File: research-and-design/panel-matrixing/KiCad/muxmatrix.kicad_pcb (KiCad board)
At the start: 2 copper layers, 112 parts, among them P1 CONN_01X03, P10 CONN_01X03, P11 CONN_01X03, P12 CONN_01X03, P13 CONN_01X03, P14 CONN_01X03, P15 CONN_01X03, P16 CONN_01X03, P17 CONN_01X03, P18 CONN_01X03, P19 CONN_01X03, P2 CONN_01X03, P20 CONN_01X03, P21 CONN_01X07, P22 CONN_01X03, P23 CONN_01X03, P24 CONN_01X03, P25 CONN_01X03, P26 CONN_01X03, P27 CONN_01X03, P28 CONN_01X03, P29 CONN_01X03, P3 CONN_01X03, P30 CONN_01X03, P31 CONN_01X03, P32 CONN_01X03, P33 CONN_01X03, P4 CONN_01X03, P5 CONN_01X03, P6 CONN_01X03, P7 CONN_01X03, P8 CONN_01X03, P9 CONN_01X03, U1 4052, U10 4052, U2 4052, U3 4052, U4 4052, U5 4052, U6 4052, U7 4052, U8 4052, U9 4052

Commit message: worked on layout
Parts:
- removed U10, U6, U7, U8, U9: 4052, SMD_Packages:SO-16-L
- P21: value CONN_01X07 -> CONN_01X03
- P33: value CONN_01X03 -> CONN_01X07
- U1, U2, U3, U4, U5: footprint SMD_Packages:SO-16-L -> SMD_Packages:SO-16-N
- moved U1 146.1 mm to (207.0, 31.8)
- moved U2 134.6 mm to (218.4, 33.0)
- moved U3 121.9 mm to (229.9, 33.0)
- moved U4 109.2 mm to (241.3, 31.8)
- moved U5 100.3 mm to (252.7, 31.8)
- moved C1 44.5 mm to (243.8, 62.2)
- moved C3 44.5 mm to (243.8, 59.7)
- moved C4 44.5 mm to (243.8, 53.3)
- moved C5 44.5 mm to (243.8, 50.8)
- moved C2 44.4 mm to (243.8, 55.9)
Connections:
- P10 pad 2: K21 -> K10
- P11 pad 2: K6 -> K11
- P12 pad 2: K22 -> K12
- P13 pad 2: K7 -> K13
- P14 pad 2: K23 -> K14
- P15 pad 2: K8 -> K15
- P16 pad 2: K24 -> K16
- P17 pad 2: K9 -> K17
- P18 pad 2: K25 -> K18
- P19 pad 2: K10 -> K19
- P2 pad 2: K17 -> K2
- P20 pad 2: K26 -> K20
- P21 pad 1: VDD -> Net-(P21-Pad1)
- P21 pad 2: GND -> K21
- P21 pad 3: A0 -> Net-(P21-Pad3)
- P21 pad 4: A1 -> (no net)
- P21 pad 5: EN -> (no net)
- P21 pad 6: A -> (no net)
- P21 pad 7: B -> (no net)
- P22 pad 2: K11 -> K22
- P23 pad 2: K27 -> K23
- P24 pad 2: K12 -> K24
- P25 pad 2: K28 -> K25
- P26 pad 2: K13 -> K26
- P27 pad 2: K29 -> K27
- P28 pad 2: K14 -> K28
- P29 pad 2: K30 -> K29
- P3 pad 2: K2 -> K3
- P30 pad 2: K15 -> K30
- P32 pad 2: K16 -> K32
- P33 pad 1: Net-(P33-Pad1) -> VDD
- P33 pad 2: K32 -> GND
- P33 pad 3: Net-(P33-Pad3) -> A0
- P4 pad 2: K18 -> K4
- P5 pad 2: K3 -> K5
- P6 pad 2: K19 -> K6
- P7 pad 2: K4 -> K7
- P8 pad 2: K20 -> K8
- P9 pad 2: K5 -> K9
- R10 pad 1: Net-(P5-Pad1) -> VDD
- R10 pad 2: GND -> Net-(P10-Pad3)
- R11 pad 2: Net-(P6-Pad3) -> Net-(P11-Pad3)
- R12 pad 1: Net-(P6-Pad1) -> VDD
- R12 pad 2: GND -> Net-(P12-Pad3)
- R13 pad 2: Net-(P7-Pad3) -> Net-(P13-Pad3)
- R14 pad 1: Net-(P7-Pad1) -> VDD
- R14 pad 2: GND -> Net-(P14-Pad3)
- R15 pad 2: Net-(P8-Pad3) -> Net-(P15-Pad3)
- R16 pad 1: Net-(P8-Pad1) -> VDD
- R16 pad 2: GND -> Net-(P16-Pad3)
- R17 pad 1: VDD -> Net-(P1-Pad1)
- R17 pad 2: Net-(P9-Pad3) -> GND
- R18 pad 1: Net-(P9-Pad1) -> Net-(P2-Pad1)
- R19 pad 1: VDD -> Net-(P3-Pad1)
- R19 pad 2: Net-(P10-Pad3) -> GND
- R2 pad 1: Net-(P1-Pad1) -> VDD
- R2 pad 2: GND -> Net-(P2-Pad3)
- R20 pad 1: Net-(P10-Pad1) -> Net-(P4-Pad1)
- R21 pad 1: VDD -> Net-(P5-Pad1)
- R21 pad 2: Net-(P11-Pad3) -> GND
- R22 pad 1: Net-(P11-Pad1) -> Net-(P6-Pad1)
- R23 pad 1: VDD -> Net-(P7-Pad1)
- R23 pad 2: Net-(P12-Pad3) -> GND
- R24 pad 1: Net-(P12-Pad1) -> Net-(P8-Pad1)
- R25 pad 1: VDD -> Net-(P9-Pad1)
- R25 pad 2: Net-(P13-Pad3) -> GND
- R26 pad 1: Net-(P13-Pad1) -> Net-(P10-Pad1)
- R27 pad 1: VDD -> Net-(P11-Pad1)
- R27 pad 2: Net-(P14-Pad3) -> GND
- R28 pad 1: Net-(P14-Pad1) -> Net-(P12-Pad1)
- R29 pad 1: VDD -> Net-(P13-Pad1)
- R29 pad 2: Net-(P15-Pad3) -> GND
- R3 pad 2: Net-(P2-Pad3) -> Net-(P3-Pad3)
- R30 pad 1: Net-(P15-Pad1) -> Net-(P14-Pad1)
- R31 pad 1: VDD -> Net-(P15-Pad1)
- R31 pad 2: Net-(P16-Pad3) -> GND
- R34 pad 1: Net-(P17-Pad1) -> VDD
- R34 pad 2: GND -> Net-(P18-Pad3)
- R35 pad 2: Net-(P18-Pad3) -> Net-(P19-Pad3)
- R36 pad 1: Net-(P18-Pad1) -> VDD
- R36 pad 2: GND -> Net-(P20-Pad3)
- R37 pad 2: Net-(P19-Pad3) -> Net-(P21-Pad3)
- R38 pad 1: Net-(P19-Pad1) -> VDD
- R38 pad 2: GND -> Net-(P22-Pad3)
- R39 pad 2: Net-(P20-Pad3) -> Net-(P23-Pad3)
- R4 pad 1: Net-(P2-Pad1) -> VDD
- R4 pad 2: GND -> Net-(P4-Pad3)
- R40 pad 1: Net-(P20-Pad1) -> VDD
- R40 pad 2: GND -> Net-(P24-Pad3)
- R41 pad 2: Net-(P22-Pad3) -> Net-(P25-Pad3)
- R42 pad 1: Net-(P22-Pad1) -> VDD
- R42 pad 2: GND -> Net-(P26-Pad3)
- R43 pad 2: Net-(P23-Pad3) -> Net-(P27-Pad3)
- R44 pad 1: Net-(P23-Pad1) -> VDD
- R44 pad 2: GND -> Net-(P28-Pad3)
- R45 pad 2: Net-(P24-Pad3) -> Net-(P29-Pad3)
- R46 pad 1: Net-(P24-Pad1) -> VDD
- R46 pad 2: GND -> Net-(P30-Pad3)
- R47 pad 2: Net-(P25-Pad3) -> Net-(P31-Pad3)
- R48 pad 1: Net-(P25-Pad1) -> VDD
- R48 pad 2: GND -> Net-(P32-Pad3)
- R49 pad 1: VDD -> Net-(P17-Pad1)
- R49 pad 2: Net-(P26-Pad3) -> GND
- R5 pad 2: Net-(P3-Pad3) -> Net-(P5-Pad3)
- R50 pad 1: Net-(P26-Pad1) -> Net-(P18-Pad1)
- R51 pad 1: VDD -> Net-(P19-Pad1)
- R51 pad 2: Net-(P27-Pad3) -> GND
- R52 pad 1: Net-(P27-Pad1) -> Net-(P20-Pad1)
- R53 pad 1: VDD -> Net-(P21-Pad1)
- R53 pad 2: Net-(P28-Pad3) -> GND
- R54 pad 1: Net-(P28-Pad1) -> Net-(P22-Pad1)
- R55 pad 1: VDD -> Net-(P23-Pad1)
- R55 pad 2: Net-(P29-Pad3) -> GND
- R56 pad 1: Net-(P29-Pad1) -> Net-(P24-Pad1)
- R57 pad 1: VDD -> Net-(P25-Pad1)
- R57 pad 2: Net-(P30-Pad3) -> GND
- R58 pad 1: Net-(P30-Pad1) -> Net-(P26-Pad1)
- R59 pad 1: VDD -> Net-(P27-Pad1)
- R59 pad 2: Net-(P31-Pad3) -> GND
- R6 pad 1: Net-(P3-Pad1) -> VDD
- R6 pad 2: GND -> Net-(P6-Pad3)
- R60 pad 1: Net-(P31-Pad1) -> Net-(P28-Pad1)
- R61 pad 1: VDD -> Net-(P29-Pad1)
- R61 pad 2: Net-(P32-Pad3) -> GND
- R62 pad 1: Net-(P32-Pad1) -> Net-(P30-Pad1)
- R63 pad 1: VDD -> Net-(P31-Pad1)
- R63 pad 2: Net-(P33-Pad3) -> GND
- R64 pad 1: Net-(P33-Pad1) -> Net-(P32-Pad1)
- R7 pad 2: Net-(P4-Pad3) -> Net-(P7-Pad3)
- R8 pad 1: Net-(P4-Pad1) -> VDD
- R8 pad 2: GND -> Net-(P8-Pad3)
- R9 pad 2: Net-(P5-Pad3) -> Net-(P9-Pad3)
- U2 pad 1: K5 -> K13
- U2 pad 11: K4 -> K12
- U2 pad 12: K1 -> K9
- U2 pad 13: OUT1 -> OUT3
- U2 pad 14: K2 -> K10
- U2 pad 15: K3 -> K11
- U2 pad 2: K7 -> K15
- U2 pad 3: OUT2 -> OUT4
- U2 pad 4: K8 -> K16
- U2 pad 5: K6 -> K14
- U3 pad 1: OUT5 -> K21
- U3 pad 11: OUT4 -> K20
- U3 pad 12: OUT1 -> K17
- U3 pad 13: A0 -> OUT5
- U3 pad 14: OUT2 -> K18
- U3 pad 15: OUT3 -> K19
- U3 pad 2: OUT7 -> K23
- U3 pad 3: A1 -> OUT6
- U3 pad 4: OUT8 -> K24
- U3 pad 5: OUT6 -> K22
- U4 pad 1: OUT5 -> K29
- U4 pad 11: OUT4 -> K28
- U4 pad 12: OUT1 -> K25
- U4 pad 13: A0 -> OUT7
- U4 pad 14: OUT2 -> K26
- U4 pad 15: OUT3 -> K27
- U4 pad 2: OUT7 -> K31
- U4 pad 3: A1 -> OUT8
- U4 pad 4: OUT8 -> K32
- U4 pad 5: OUT6 -> K30
- U5 pad 1: K13 -> OUT5
- U5 pad 11: K12 -> OUT4
- U5 pad 12: K9 -> OUT1
- U5 pad 13: OUT3 -> A0
- U5 pad 14: K10 -> OUT2
- U5 pad 15: K11 -> OUT3
- U5 pad 2: K15 -> OUT7
- U5 pad 3: OUT4 -> A1
- U5 pad 4: K16 -> OUT8
- U5 pad 5: K14 -> OUT6
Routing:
- net Net-(P33-Pad3): track 22.0 -> 0.00 mm
- net GND: track 0.00 -> 21.8 mm
- net Net-(P33-Pad1): track 13.9 -> 0.00 mm
- net VDD: track 0.00 -> 12.7 mm
- net Net-(P32-Pad3): track 13.5 -> 1.91 mm
- net Net-(P30-Pad1): track 0.00 -> 11.5 mm
- net Net-(P32-Pad1): track 13.4 -> 3.20 mm
- net A0: track 0.00 -> 7.34 mm

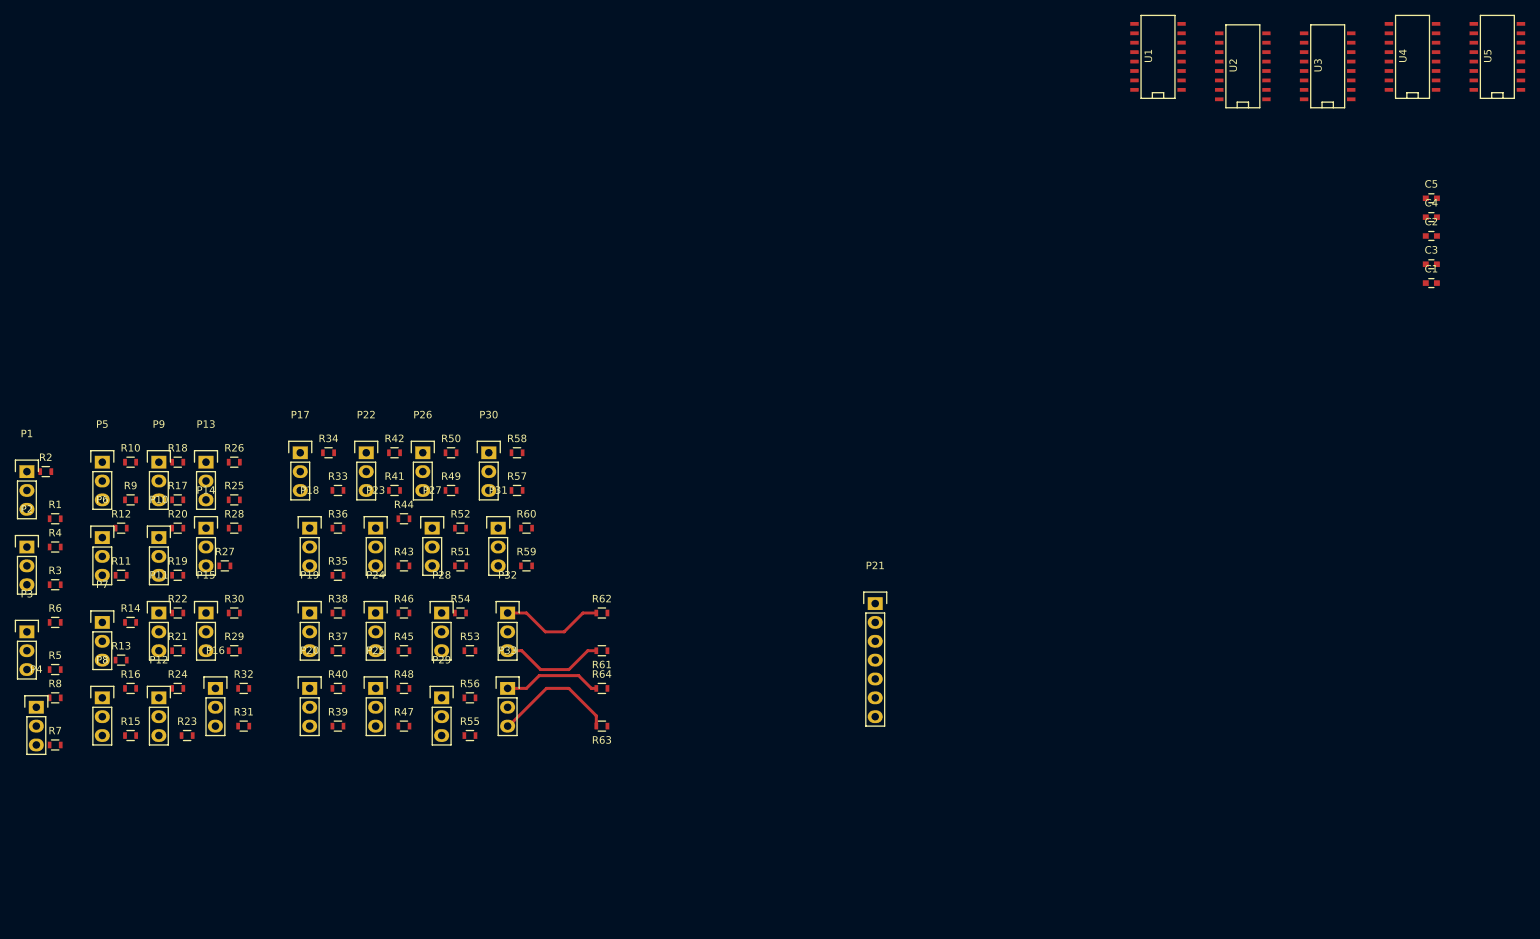
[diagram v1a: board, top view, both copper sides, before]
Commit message: Testing out new dual trimpot footprint
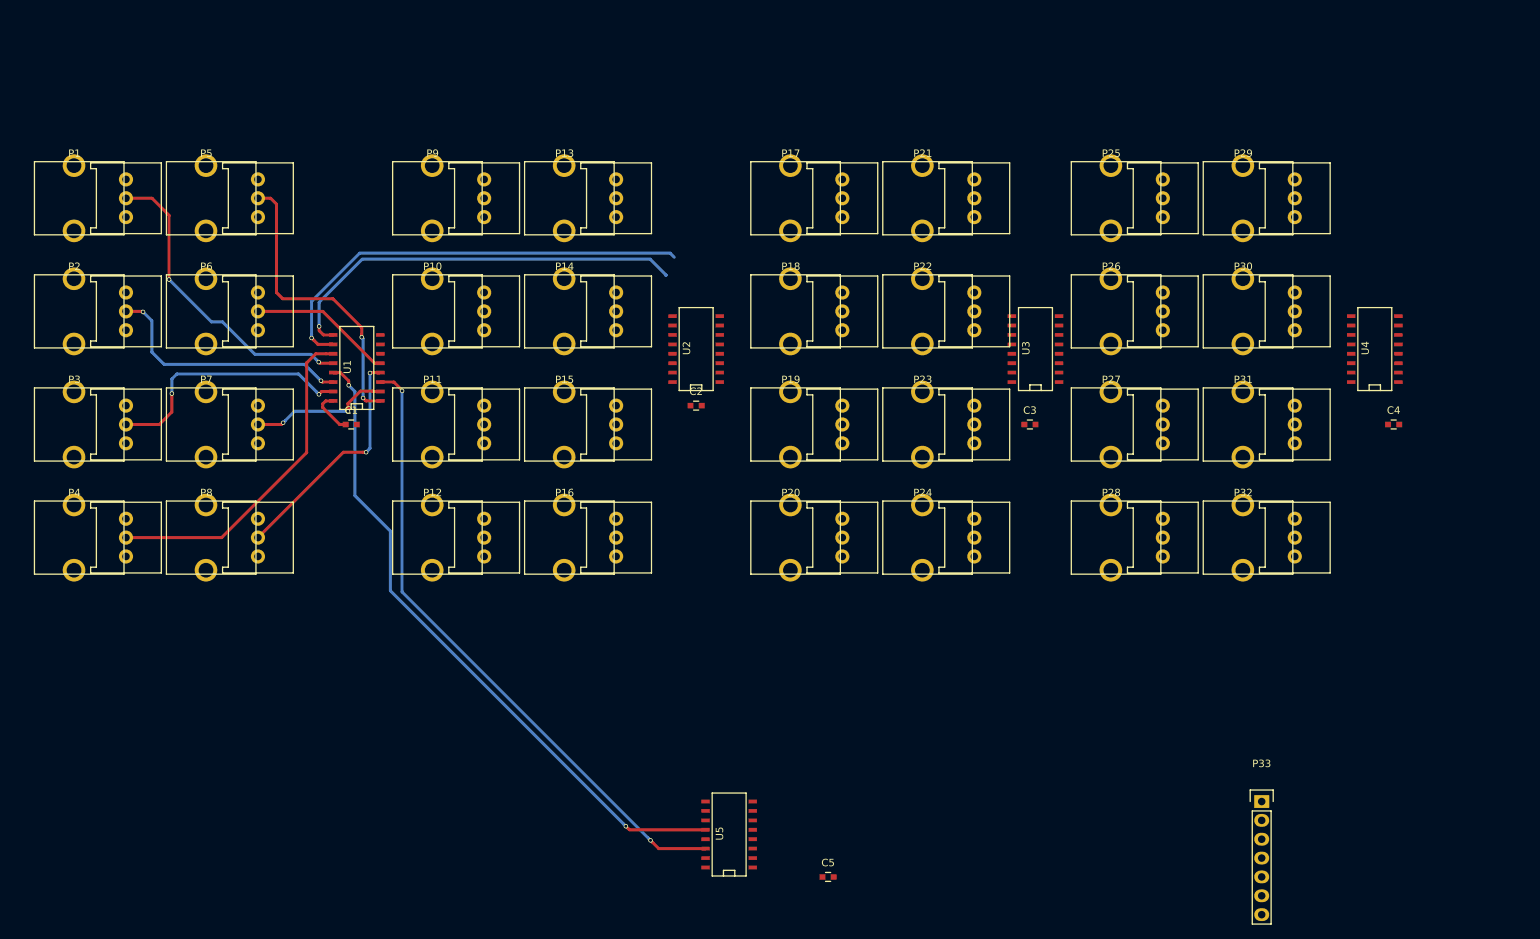
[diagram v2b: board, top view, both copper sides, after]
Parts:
- removed R1, R10, R11, R12, R13, R14, R15, R16, R17, R18, R19, R2, R20, R21, R22, R23, R24, R25, R26, R27, R28, R29, R3, R30, R31, R32, R33, R34, R35, R36, R37, R38, R39, R4, R40, R41, R42, R43, R44, R45, R46, R47, R48, R49, R5, R50, R51, R52, R53, R54, R55, R56, R57, R58, R59, R6, R60, R61, R62, R63, R64, R7, R8, R9: 1K, Resistors_SMD:R_0603
- P1, P10, P11, P12, P13, P14, P15, P16, P17, P18, P19, P2, P20, P22, P23, P24, P25, P26, P27, P28, P29, P3, P30, P31, P32, P4, P5, P6, P7, P8, P9: footprint Pin_Headers:Pin_Header_Straight_1x03 -> trytwo:dualpot
- P21: footprint Pin_Headers:Pin_Header_Straight_1x07 -> trytwo:dualpot
- P33: footprint Pin_Headers:Pin_Header_Straight_1x03 -> Pin_Headers:Pin_Header_Straight_1x07
- moved U5 147.3 mm to (149.2, 136.5)
- moved C1 146.8 mm to (98.3, 81.3)
- moved P29 127.2 mm to (218.4, 50.8)
- moved C5 122.3 mm to (162.6, 142.2)
- moved P25 119.1 mm to (200.7, 50.8)
- moved U1 115.8 mm to (99.1, 73.7)
- moved P30 103.4 mm to (218.4, 66.0)
- moved P33 102.7 mm to (221.0, 132.1)
- moved C2 101.7 mm to (144.8, 78.7)
- moved P31 101.3 mm to (218.4, 81.3)
- moved P32 99.6 mm to (218.4, 96.5)
- moved P26 94.6 mm to (200.7, 66.0)
- moved P27 92.5 mm to (200.7, 81.3)
- moved P28 90.7 mm to (200.7, 96.5)
- moved U2 82.9 mm to (144.8, 71.1)
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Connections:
- P1 pad 1: Net-(P1-Pad1) -> GND
- P1 pad 3: Net-(P1-Pad3) -> VDD
- P10 pad 1: Net-(P10-Pad1) -> GND
- P10 pad 3: Net-(P10-Pad3) -> VDD
- P11 pad 1: Net-(P11-Pad1) -> GND
- P11 pad 3: Net-(P11-Pad3) -> VDD
- P12 pad 1: Net-(P12-Pad1) -> GND
- P12 pad 3: Net-(P12-Pad3) -> VDD
- P13 pad 1: Net-(P13-Pad1) -> GND
- P13 pad 3: Net-(P13-Pad3) -> VDD
- P14 pad 1: Net-(P14-Pad1) -> GND
- P14 pad 3: Net-(P14-Pad3) -> VDD
- P15 pad 1: Net-(P15-Pad1) -> GND
- P15 pad 3: Net-(P15-Pad3) -> VDD
- P16 pad 1: Net-(P16-Pad1) -> GND
- P16 pad 3: Net-(P16-Pad3) -> VDD
- P17 pad 1: Net-(P17-Pad1) -> GND
- P17 pad 3: Net-(P17-Pad3) -> VDD
- P18 pad 1: Net-(P18-Pad1) -> GND
- P18 pad 3: Net-(P18-Pad3) -> VDD
- P19 pad 1: Net-(P19-Pad1) -> GND
- P19 pad 3: Net-(P19-Pad3) -> VDD
- P2 pad 1: Net-(P2-Pad1) -> GND
- P2 pad 3: Net-(P2-Pad3) -> VDD
- P20 pad 1: Net-(P20-Pad1) -> GND
- P20 pad 3: Net-(P20-Pad3) -> VDD
- P21 pad 1: Net-(P21-Pad1) -> GND
- P21 pad 3: Net-(P21-Pad3) -> VDD
- P22 pad 1: Net-(P22-Pad1) -> GND
- P22 pad 3: Net-(P22-Pad3) -> VDD
- P23 pad 1: Net-(P23-Pad1) -> GND
- P23 pad 3: Net-(P23-Pad3) -> VDD
- P24 pad 1: Net-(P24-Pad1) -> GND
- P24 pad 3: Net-(P24-Pad3) -> VDD
- P25 pad 1: Net-(P25-Pad1) -> GND
- P25 pad 3: Net-(P25-Pad3) -> VDD
- P26 pad 1: Net-(P26-Pad1) -> GND
- P26 pad 3: Net-(P26-Pad3) -> VDD
- P27 pad 1: Net-(P27-Pad1) -> GND
- P27 pad 3: Net-(P27-Pad3) -> VDD
- P28 pad 1: Net-(P28-Pad1) -> GND
- P28 pad 3: Net-(P28-Pad3) -> VDD
- P29 pad 1: Net-(P29-Pad1) -> GND
- P29 pad 3: Net-(P29-Pad3) -> VDD
- P3 pad 1: Net-(P3-Pad1) -> GND
- P3 pad 3: Net-(P3-Pad3) -> VDD
- P30 pad 1: Net-(P30-Pad1) -> GND
- P30 pad 3: Net-(P30-Pad3) -> VDD
- P31 pad 1: Net-(P31-Pad1) -> GND
- P31 pad 3: Net-(P31-Pad3) -> VDD
- P32 pad 1: Net-(P32-Pad1) -> GND
- P32 pad 3: Net-(P32-Pad3) -> VDD
- P4 pad 1: Net-(P4-Pad1) -> GND
- P4 pad 3: Net-(P4-Pad3) -> VDD
- P5 pad 1: Net-(P5-Pad1) -> GND
- P5 pad 3: Net-(P5-Pad3) -> VDD
- P6 pad 1: Net-(P6-Pad1) -> GND
- P6 pad 3: Net-(P6-Pad3) -> VDD
- P7 pad 1: Net-(P7-Pad1) -> GND
- P7 pad 3: Net-(P7-Pad3) -> VDD
- P8 pad 1: Net-(P8-Pad1) -> GND
- P8 pad 3: Net-(P8-Pad3) -> VDD
- P9 pad 1: Net-(P9-Pad1) -> GND
- P9 pad 3: Net-(P9-Pad3) -> VDD
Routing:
- net OUT1: track 0.00 -> 89.0 mm, vias 0 -> 2
- net OUT2: track 0.00 -> 85.8 mm, vias 0 -> 2
- net A: track 0.00 -> 60.0 mm, vias 0 -> 1
- net B: track 0.00 -> 56.1 mm, vias 0 -> 1
- net K4: track 0.00 -> 45.3 mm
- net K1: track 0.00 -> 42.2 mm, vias 0 -> 2
- net K5: track 0.00 -> 40.2 mm, vias 0 -> 2
- net K3: track 0.00 -> 34.6 mm, vias 0 -> 2
- net K2: track 0.00 -> 34.3 mm, vias 0 -> 2
- net K8: track 0.00 -> 31.6 mm, vias 0 -> 2
- net GND: track 21.8 -> 0.00 mm
- net K6: track 0.00 -> 19.4 mm
- net K7: track 0.00 -> 19.0 mm, vias 0 -> 2
- net Net-(P30-Pad1): track 11.5 -> 0.00 mm
- net A0: track 7.34 -> 0.15 mm
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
